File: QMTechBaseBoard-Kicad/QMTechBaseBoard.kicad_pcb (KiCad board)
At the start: 2 copper layers, 170 x 170 mm, 71 parts, among them J1 OLED-FPGA1, J10 Conn_02x32_Odd_Even, J11 Micro_SD_Card, J12 Conn_02x32_Odd_Even, J13 Conn_01x06_Female, J14 JTAG-FPGA2, J15 Micro_SD_Card, J16 Conn_02x32_Odd_Even, J17 OLED-FPGA2, J21 USB_B_Micro, J3 Stereo Audio, J5 Power-Internal, J6 Barrel_Jack_Switch, J7 JTAG-FPGA1, J8 Conn_02x32_Odd_Even, J9 Conn_01x06_Female, SW1 SW_Push, SW10 SW_Push, SW11 SW_Push, SW12 SW_Push, SW13 SW_DIP_x02, SW14 SW_DIP_x02, SW2 SW_Push, SW3 SW_Push, SW4 SW_Push, SW5 SW_Push, SW6 SW_Push, SW7 SW_Push, SW8 SW_Push, SW9 SW_Push, U1 FT4232H, U2 RTL8211EG-VB-CG, U3 RTL8211EG-VB-CG

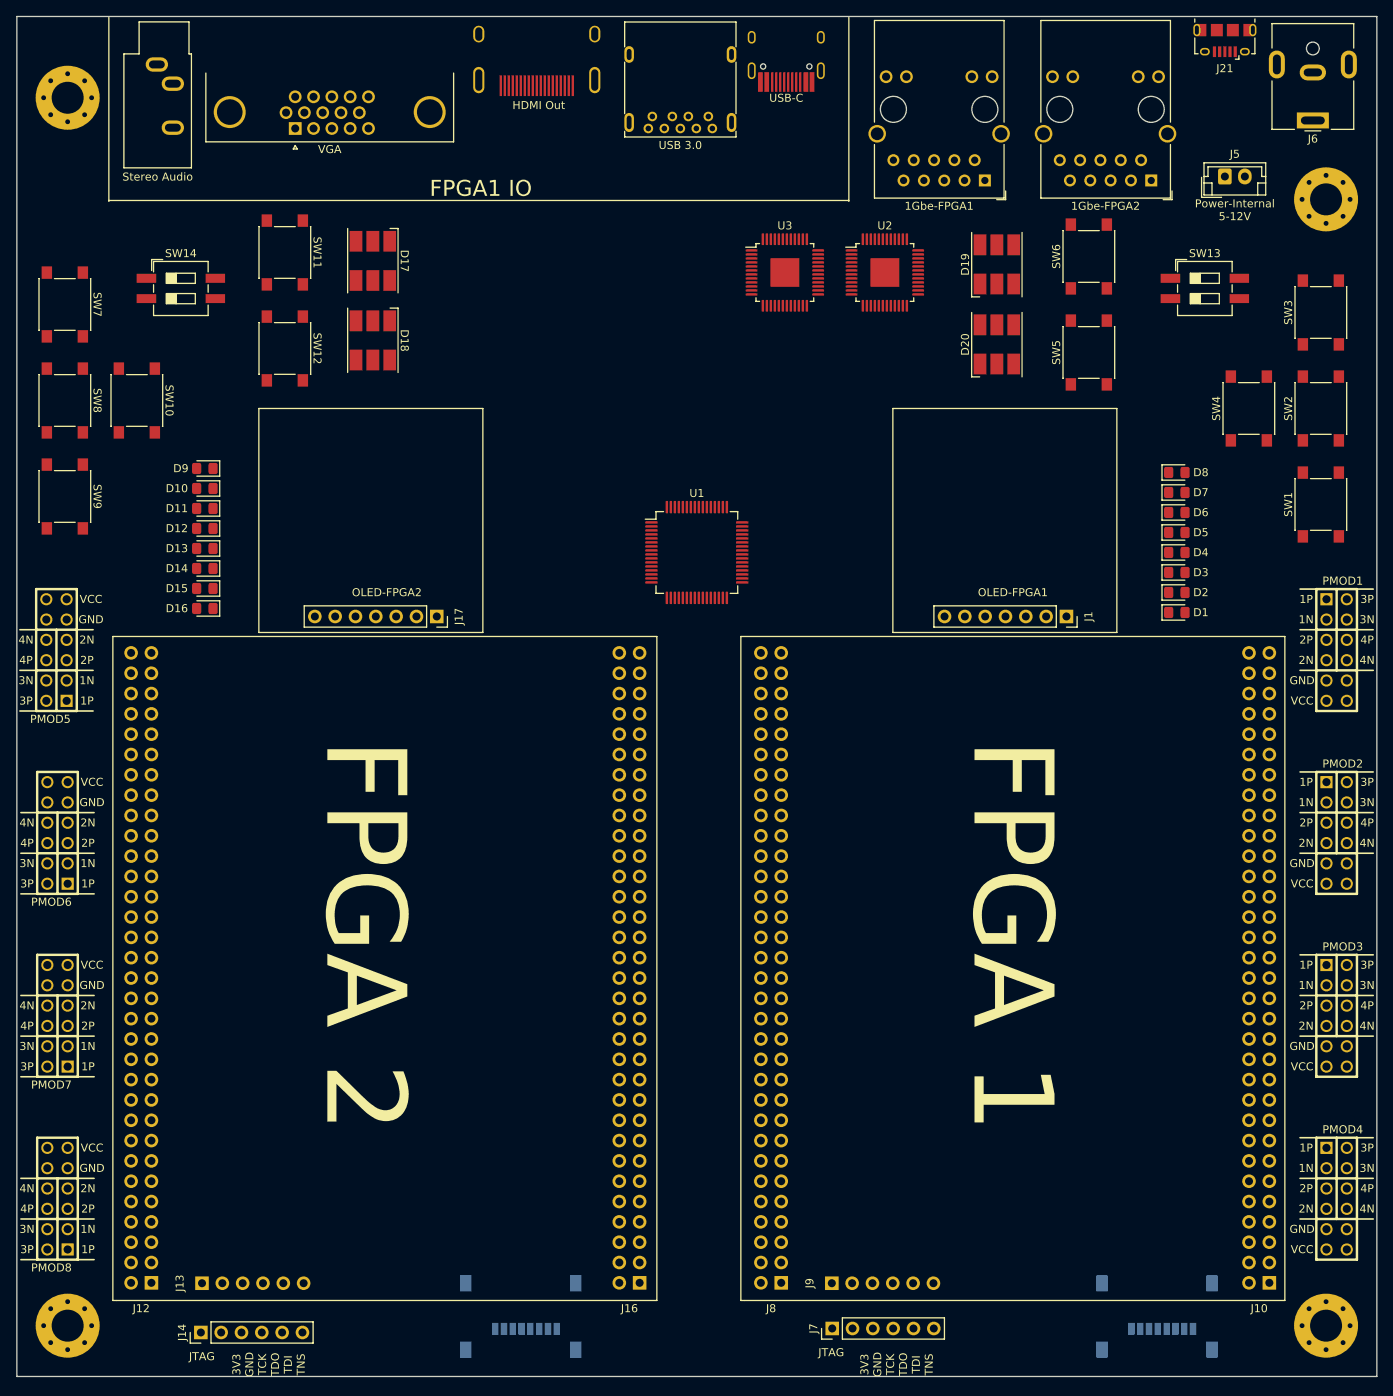
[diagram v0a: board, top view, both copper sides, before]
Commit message: Fix some text. Update draft board render
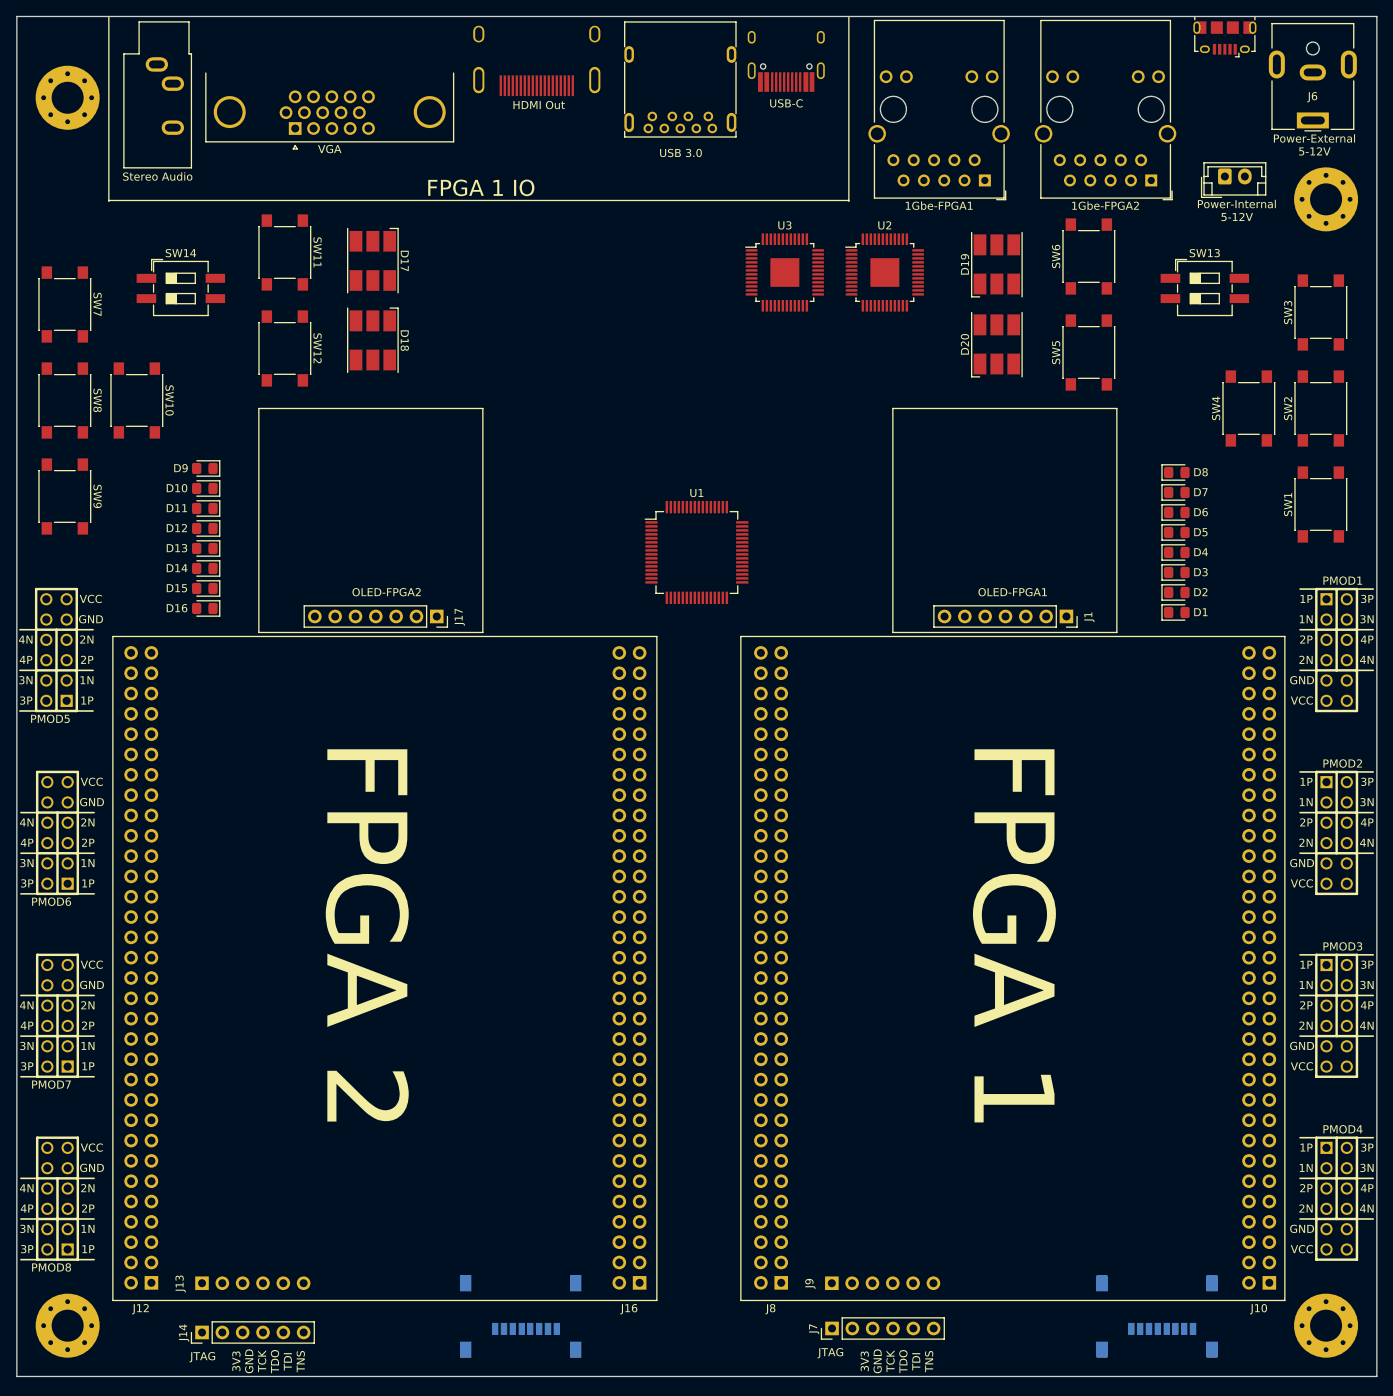
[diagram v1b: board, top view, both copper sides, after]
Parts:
- 1Gbe-FPGA2: value 1Gbe-FPGA1 -> 1Gbe-FPGA2
- J21: value USB_B_Micro -> UART-JTAG
- J6: value Barrel_Jack_Switch -> Power-External
- moved J21 0.30 mm to (216.6, 74.2)
- moved J14 0.15 mm to (88.7, 236.0)
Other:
- board text added: "FPGA 1 IO"
- board text added: "Power-External 5-12V"
- board text added: "Power-Internal 5-12V"
- board text removed: "FPGA1 IO"
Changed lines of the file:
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@@
       (effects (font (size 1 1) (thickness 0.15)))
     )
-    (fp_text value "MountingHole_4mm_Pad_Via" (at 0 5) (layer "F.Fab")
+    (fp_text value "MountingHole_4mm_Pad_Via" (at 0 5) (layer "F.Fab") hide
       (effects (font (size 1 1) (thickness 0.15)))
     )
@@
       (effects (font (size 1 1) (thickness 0.15)))
     )
-    (fp_text value "MountingHole_4mm_Pad_Via" (at 0 5) (layer "F.Fab")
+    (fp_text value "MountingHole_4mm_Pad_Via" (at 0 5) (layer "F.Fab") hide
       (effects (font (size 1 1) (thickness 0.15)))
     )
@@
       (effects (font (size 1 1) (thickness 0.15)))
     )
-    (fp_text value "MountingHole_4mm_Pad_Via" (at 0 5) (layer "F.Fab")
+    (fp_text value "MountingHole_4mm_Pad_Via" (at 0 5) (layer "F.Fab") hide
       (effects (font (size 1 1) (thickness 0.15)))
     )
@@
       (effects (font (size 1 1) (thickness 0.15)))
     )
-    (fp_text value "MountingHole_4mm_Pad_Via" (at 0 5) (layer "F.Fab")
+    (fp_text value "MountingHole_4mm_Pad_Via" (at 0 5) (layer "F.Fab") hide
       (effects (font (size 1 1) (thickness 0.15)))
     )
@@
     (tags "barrel jack cui dc power")
     (attr through_hole)
-    (fp_text reference "J6" (at 0 -2.3) (layer "F.SilkS")
+    (fp_text reference "J6" (at 0 3) (layer "F.SilkS")
       (effects (font (size 1 1) (thickness 0.15)))
     )
-    (fp_text value "Barrel_Jack_Switch" (at 0 13) (layer "F.Fab")
+    (fp_text value "Power-External" (at -0.1 -2.4) (layer "F.Fab") hide
       (effects (font (size 1 1) (thickness 0.15)))
     )
@@
   )
   (footprint "Connector_PinHeader_2.54mm:PinHeader_1x06_P2.54mm_Vertical" (layer "F.Cu")
-    (at 88.559999 236.000001 90)
+    (at 88.709999 236.000001 90)
     (descr "Through hole straight pin header, 1x06, 2.54mm pitch, single row")
     (tags "Through hole pin header THT 1x06 2.54mm single row")
@@
       (effects (font (size 1 1) (thickness 0.15)))
     )
-    (fp_text value "JTAG-FPGA2" (at 0 15.03 90) (layer "F.Fab")
+    (fp_text value "JTAG-FPGA2" (at 2.95 15.65 90) (layer "F.Fab")
       (effects (font (size 1 1) (thickness 0.15)))
     )
@@
   )
   (footprint "Connector_PinHeader_2.54mm:PinHeader_1x06_P2.54mm_Vertical" (layer "F.Cu")
-    (at 167.479999 235.500001 90)
+    (at 167.459999 235.500001 90)
     (descr "Through hole straight pin header, 1x06, 2.54mm pitch, single row")
     (tags "Through hole pin header THT 1x06 2.54mm single row")
@@
       (effects (font (size 1 1) (thickness 0.15)))
     )
-    (fp_text value "JTAG-FPGA1" (at 0 15.03 90) (layer "F.Fab")
+    (fp_text value "JTAG-FPGA1" (at 2.7 15.6 90) (layer "F.Fab")
       (effects (font (size 1 1) (thickness 0.15)))
     )
@@
       (effects (font (size 1 1) (thickness 0.15)))
     )
-    (fp_text value "DB15_Female_HighDensity" (at -4.315 14.89) (layer "F.Fab")
+    (fp_text value "DB15_Female_HighDensity" (at -4.315 14.89) (layer "F.Fab") hide
       (effects (font (size 1 1) (thickness 0.15)))
     )
@@
     (tags "connector JST EH vertical")
     (attr through_hole)
-    (fp_text reference "J5" (at 1.25 -2.8) (layer "F.SilkS")
+    (fp_text reference "J5" (at 1.25 -2.8) (layer "F.SilkS") hide
       (effects (font (size 1 1) (thickness 0.15)))
     )
-    (fp_text value "Power-Internal" (at 1.25 3.4) (layer "F.SilkS")
-      (effects (font (size 1 1) (thickness 0.15)))
-    )
-    (fp_text user "5-12V" (at 1.25 5 unlocked) (layer "F.SilkS")
+    (fp_text value "Power-Internal" (at 1.25 3.4) (layer "F.SilkS") hide
       (effects (font (size 1 1) (thickness 0.15)))
     )
@@
     (tags "USB 3.0 type A right angle")
     (attr through_hole)
-    (fp_text reference "USB 3.0" (at 3.5 -3.6) (layer "F.SilkS")
+    (fp_text reference "USB 3.0" (at 3.435 -4.6) (layer "F.SilkS")
       (effects (font (size 1 1) (thickness 0.15)))
     )
-    (fp_text value "USB3_A" (at 3.5 13) (layer "F.Fab")
+    (fp_text value "USB3_A" (at 3.5 13) (layer "F.Fab") hide
       (effects (font (size 1 1) (thickness 0.15)))
     )
@@
     (at 161.734998 71.500001 180)
     (attr smd)
-    (fp_text reference "USB-C" (at 0 -10.2) (layer "F.SilkS")
+    (fp_text reference "USB-C" (at 0 -10.9) (layer "F.SilkS")
       (effects (font (size 1 1) (thickness 0.15)))
     )
-    (fp_text value "USB_C_Plug" (at 0 1.15) (layer "Dwgs.User")
+    (fp_text value "USB_C_Plug" (at 0 1.15) (layer "Dwgs.User") hide
       (effects (font (size 1 1) (thickness 0.15)))
     )
@@
   )
   (footprint "Connector_USB:USB_Micro-B_Amphenol_10118194_Horizontal" (layer "F.Cu")
-    (at 216.559999 74.500001 180)
+    (at 216.559999 74.200001 180)
     (descr "USB Micro-B receptacle, horizontal, SMD, 10118194, https://cdn.amphenol-icc.com/media/wysiwyg/files/drawing/10118194.pdf")
     (tags "USB Micro B horizontal SMD")
     (attr smd)
-    (fp_text reference "J21" (at 0 -3.5) (layer "F.SilkS")
+    (fp_text reference "J21" (at 0 -3.5) (layer "F.SilkS") hide
       (effects (font (size 1 1) (thickness 0.15)))
     )
-    (fp_text value "USB_B_Micro" (at 0 4.75) (layer "F.Fab")
+    (fp_text value "UART-JTAG" (at -0.2 -3.6) (layer "F.Fab")
       (effects (font (size 1 1) (thickness 0.15)))
     )
@@
       (effects (font (size 1 1) (thickness 0.15)))
     )
-    (fp_text value "1Gbe-FPGA1" (at 0 21.7 180) (layer "F.Fab")
+    (fp_text value "1Gbe-FPGA1" (at 0 21.7 180) (layer "F.Fab") hide
       (effects (font (size 1 1) (thickness 0.15)))
     )
@@
       (effects (font (size 1 1) (thickness 0.15)))
     )
-    (fp_text value "1Gbe-FPGA1" (at 0 21.7 180) (layer "F.Fab")
+    (fp_text value "1Gbe-FPGA2" (at 0 21.7 180) (layer "F.Fab") hide
       (effects (font (size 1 1) (thickness 0.15)))
     )
@@
   (gr_line (start 235.559999 241.500001) (end 235.559999 71.500001) (layer "Edge.Cuts") (width 0.12))
   (gr_text "FPGA 2" (at 108.993999 186.382001 -90) (layer "F.SilkS")
-    (effects (font (size 10 10) (thickness 0.15)))
+    (effects (font (size 10 10) (thickness 1)))
   )
-  (gr_text "3V3\nGND\nTCK\nTDO\nTDI\nTNS" (at 97.059999 240.000001 90) (layer "F.SilkS")
+  (gr_text "3V3\nGND\nTCK\nTDO\nTDI\nTNS" (at 97.059999 239.600001 90) (layer "F.SilkS")
     (effects (font (size 1 1) (thickness 0.15)))
   )
-  (gr_text "FPGA1 IO" (at 123.559999 93.000001) (layer "F.SilkS")
+  (gr_text "FPGA 1 IO" (at 123.559999 93.000001) (layer "F.SilkS")
     (effects (font (size 2 2) (thickness 0.15)))
   )
+  (gr_text "Power-External\n5-12V" (at 227.759999 87.600001) (layer "F.SilkS")
+    (effects (font (size 1 1) (thickness 0.15)))
+  )
   (gr_text "FPGA 1" (at 189.892999 186.382001 -90) (layer "F.SilkS")
-    (effects (font (size 10 10) (thickness 0.15)))
+    (effects (font (size 10 10) (thickness 1)))
+  )
+  (gr_text "Power-Internal\n5-12V" (at 218.059999 95.800001) (layer "F.SilkS")
+    (effects (font (size 1 1) (thickness 0.15)))
   )
-  (gr_text "3V3\nGND\nTCK\nTDO\nTDI\nTNS" (at 175.559999 240.000001 90) (layer "F.SilkS")
+  (gr_text "3V3\nGND\nTCK\nTDO\nTDI\nTNS" (at 175.609999 239.600001 90) (layer "F.SilkS")
     (effects (font (size 1 1) (thickness 0.15)))
   )
